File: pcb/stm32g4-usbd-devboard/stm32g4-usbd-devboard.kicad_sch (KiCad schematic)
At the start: 29 parts, among them J1 USB_B_Mini, J2 PIN H 6P, J3 LEFT, J4 RIGHT, J5 BOOTLOADER, U1 USBLC6-2SC6, U2 MCP1700-3302E, U3 STM32G431KBTx, Y1 24MHz

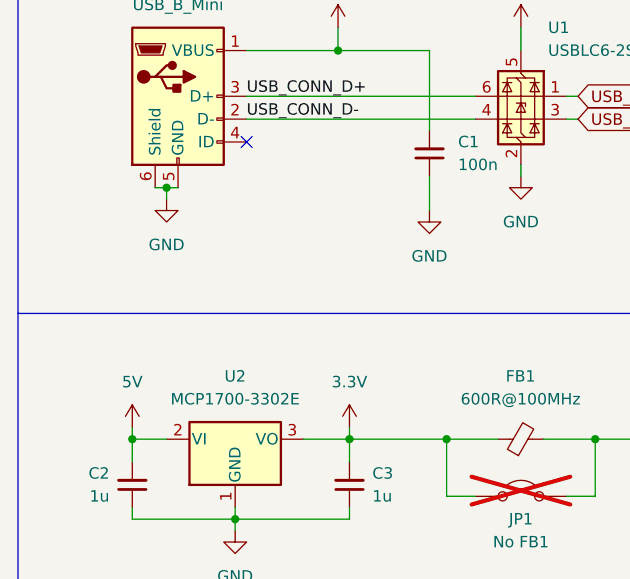
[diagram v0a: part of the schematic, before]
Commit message: pcb: g4: upgrade to kicad 10
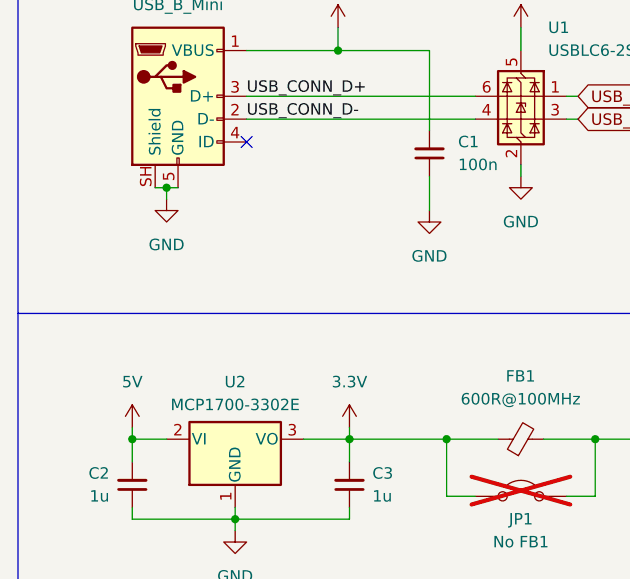
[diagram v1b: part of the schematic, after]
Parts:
- U2: symbol Regulator_Linear:MCP1700x-330xxTO -> custom:MCP1700x-330xxTO
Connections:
- net GND: now also J1.SH (Shield); no longer J1.6 (Shield)
